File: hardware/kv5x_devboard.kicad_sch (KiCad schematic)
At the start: 0 parts

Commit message: JTAG/SWD connector and pinouts
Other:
- added sheet Buttons and switches (./sch/btn_sw.kicad_sch)
- added sheet General Purpose IO (./sch/gpio.kicad_sch)
- added sheet IMU (./sch/imu.kicad_sch)
- added sheet JTAG, SWD interface (./sch/jtag_swd.kicad_sch)
- added sheet Microcontroller (./sch/mcu.kicad_sch)
- added sheet Power (./sch/power.kicad_sch)

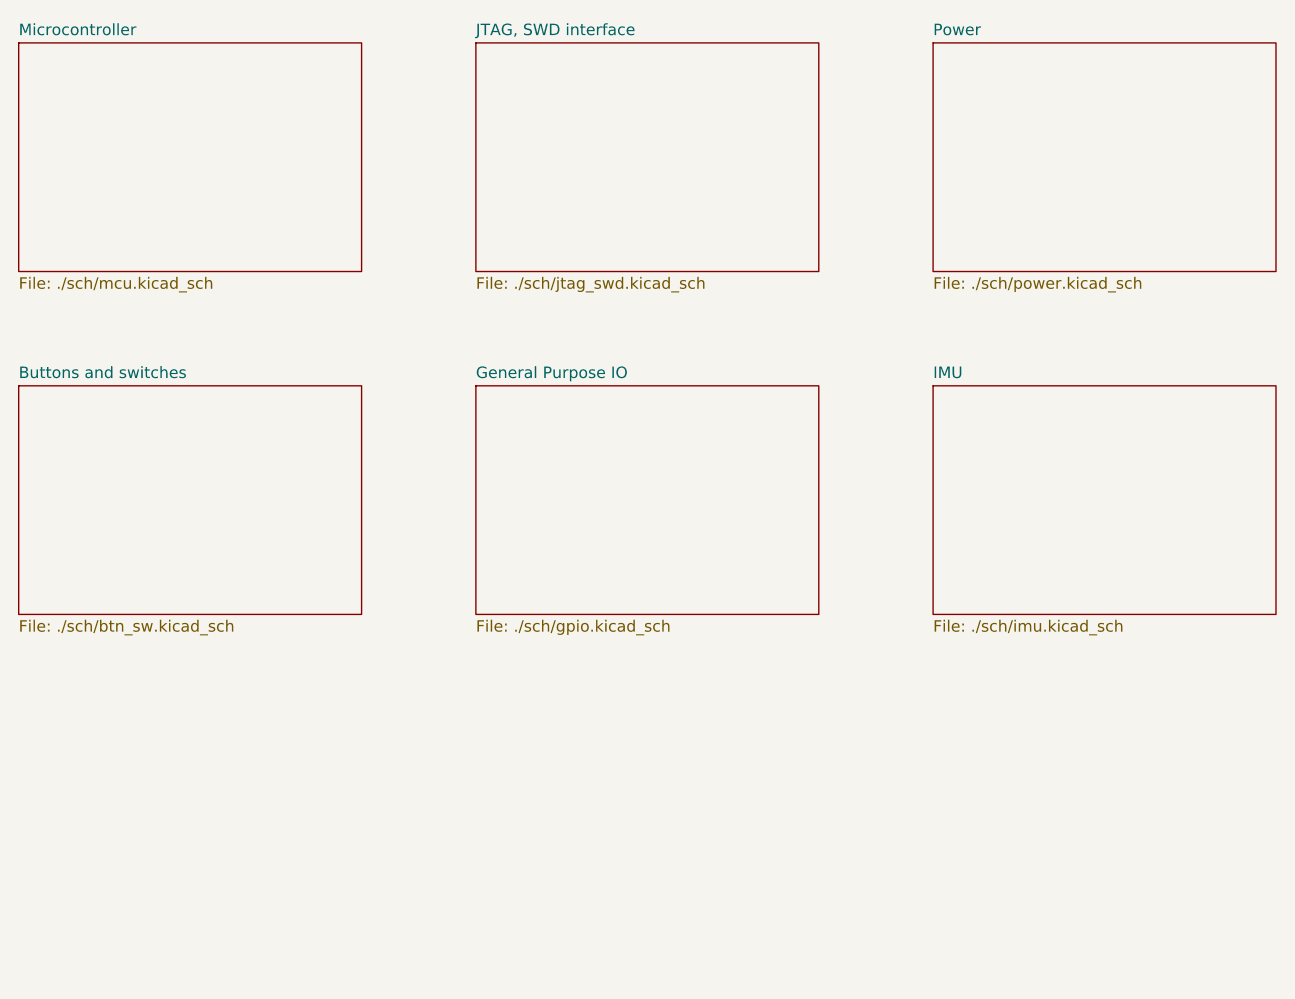
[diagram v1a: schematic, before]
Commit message: re-added USB interface because I realized I needed it
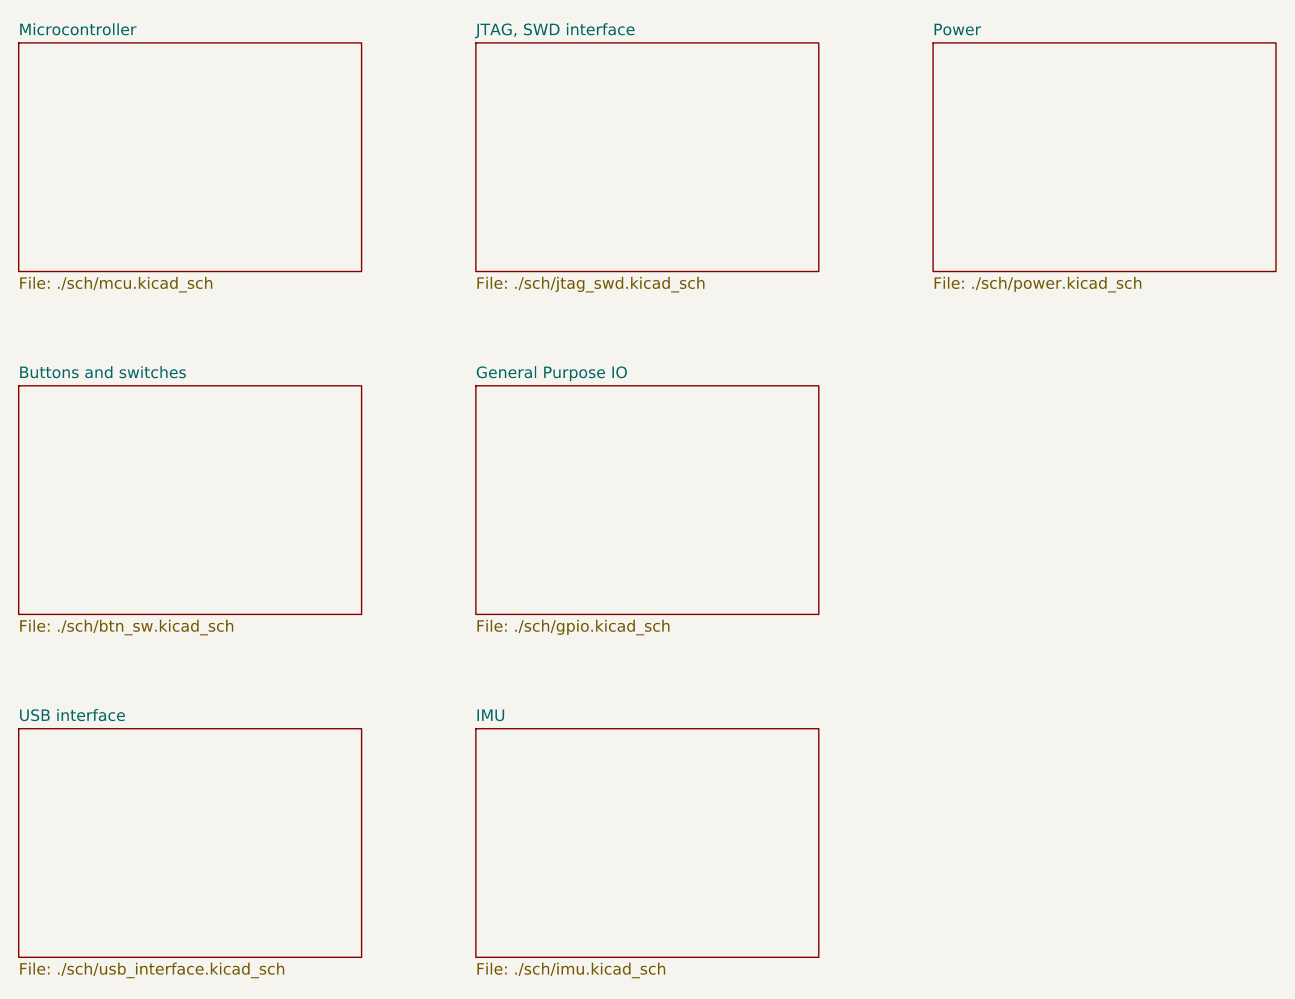
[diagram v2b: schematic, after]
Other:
- added sheet USB interface (./sch/usb_interface.kicad_sch)
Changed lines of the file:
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@@
+	)
+	(sheet
+		(at 50.8 127)
+		(size 38.1 25.4)
+		(exclude_from_sim no)
+		(in_bom yes)
+		(on_board yes)
+		(dnp no)
+		(fields_autoplaced yes)
+		(stroke
+			(width 0.1524)
+			(type solid)
+		)
+		(fill
+			(color 0 0 0 0.0000)
+		)
+		(property "Sheetname" "USB interface"
+			(at 50.8 126.2884 0)
+			(effects
+				(font
+					(size 1.27 1.27)
+				)
+				(justify left bottom)
+			)
+		)
+		(property "Sheetfile" "./sch/usb_interface.kicad_sch"
+			(at 50.8 152.9846 0)
+			(effects
+				(font
+					(size 1.27 1.27)
+				)
+				(justify left top)
+			)
+		)
+		(instances
+			(project "kv5x_devboard"
+				(path "/0d451eb2-75be-4a38-9e93-e62b45068f1d"
+					(page "8")
+				)
+			)
+		)
 	)
 	(sheet
@@
 	)
 	(sheet
-		(at 152.4 88.9)
+		(at 101.6 127)
 		(size 38.1 25.4)
 		(exclude_from_sim no)
@@
 		)
 		(property "Sheetname" "IMU"
-			(at 152.4 88.1884 0)
+			(at 101.6 126.2884 0)
 			(effects
 				(font
@@
 		)
 		(property "Sheetfile" "./sch/imu.kicad_sch"
-			(at 152.4 114.8846 0)
+			(at 101.6 152.9846 0)
 			(effects
 				(font
